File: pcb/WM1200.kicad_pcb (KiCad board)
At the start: 4 copper layers, 159 x 104 mm, 143 parts, among them Q1 BC817, Q2 BC817, Q3 BC817, Q4 BC817, Q5 BC817, Q6 BC817, U1 74LVCH162245A, U2 74LVCH162245A, U3 74LVCH162245A, U4 74LVCH162245A, U5 74LVCH162245A, U6 ADP2108AUJ-3.3, U7 TPD12S016PWR, X1 audio_expansion, X2 A1200_trapdoor_connector, X3 AC7020, X4 Conn_02x05_Odd_Even, X5 HDMI_A

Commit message: time to stop for today
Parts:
- moved C31 10.6 mm to (230.1, 111.3)
- moved R21 10.6 mm to (218.8, 113.2)
- moved R23 10.6 mm to (222.3, 122.7)
- moved C29 10.6 mm to (230.8, 120.5)
- moved C30 10.6 mm to (219.5, 119.5)
- moved C32 10.6 mm to (240.0, 108.3)
- moved R22 10.6 mm to (216.8, 116.9)
- moved R24 10.6 mm to (240.0, 106.8)
- moved R25 10.6 mm to (219.7, 116.9)
- moved U7 10.6 mm to (225.2, 116.6)
- moved X5 10.6 mm to (226.5, 113.1)
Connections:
- X3 pad J11_10: _FPGA_IPL0 -> Net-(X3-PadJ11_10)
- X3 pad J11_11: FPGA_FC1 -> Net-(X3-PadJ11_11)
- X3 pad J11_12: _FPGA_IPL1 -> Net-(X3-PadJ11_12)
- X3 pad J11_13: FPGA_FC2 -> Net-(X3-PadJ11_13)
- X3 pad J11_14: _FPGA_IPL2 -> Net-(X3-PadJ11_14)
- X3 pad J11_15: FPGA_R_W -> Net-(X3-PadJ11_15)
- X3 pad J11_16: _FPGA_RST -> Net-(X3-PadJ11_16)
- X3 pad J11_17: FPGA_SIZE0 -> Net-(X3-PadJ11_17)
- X3 pad J11_18: FPGA_CPUCLK_A -> Net-(X3-PadJ11_18)
- X3 pad J11_19: FPGA_SIZE1 -> FPGA_HDMI_D2+
- X3 pad J11_20: FPGA_OC_HLT -> Net-(X3-PadJ11_20)
- X3 pad J11_21: FPGA_HDMI_CLK- -> FPGA_HDMI_D1+
- X3 pad J11_22: FPGA_OC_INT2 -> FPGA_HDMI_D2-
- X3 pad J11_23: FPGA_HDMI_CLK+ -> FPGA_HDMI_D0+
- X3 pad J11_24: FPGA_OC_INT6 -> FPGA_HDMI_D1-
- X3 pad J11_25: FPGA_HDMI_D0- -> FPGA_HDMI_CLK+
- X3 pad J11_26: FPGA_OC_BOSS -> FPGA_HDMI_D0-
- X3 pad J11_27: FPGA_HDMI_D0+ -> Net-(X3-PadJ11_27)
- X3 pad J11_28: FPGA_OC_OVR -> FPGA_HDMI_CLK-
- X3 pad J11_29: FPGA_HDMI_D1- -> Net-(X3-PadJ11_29)
- X3 pad J11_3: FPGA_AUD_SD -> Net-(X3-PadJ11_3)
- X3 pad J11_30: FPGA_OC_RST -> Net-(X3-PadJ11_30)
- X3 pad J11_31: FPGA_HDMI_D1+ -> Net-(X3-PadJ11_31)
- X3 pad J11_32: _FPGA_DS -> Net-(X3-PadJ11_32)
- X3 pad J11_33: FPGA_HDMI_D2- -> Net-(X3-PadJ11_33)
- X3 pad J11_34: _FPGA_BERR -> Net-(X3-PadJ11_34)
- X3 pad J11_35: FPGA_HDMI_D2+ -> Net-(X3-PadJ11_35)
- X3 pad J11_36: _FPGA_AS -> Net-(X3-PadJ11_36)
- X3 pad J11_4: _FPGA_DSACK0 -> Net-(X3-PadJ11_4)
- X3 pad J11_5: FPGA_AUD_PWM_R -> Net-(X3-PadJ11_5)
- X3 pad J11_6: _FPGA_DSACK1 -> Net-(X3-PadJ11_6)
- X3 pad J11_7: FPGA_AUD_PWM_L -> Net-(X3-PadJ11_7)
- X3 pad J11_8: _FPGA_HLT -> Net-(X3-PadJ11_8)
- X3 pad J11_9: FPGA_FC0 -> Net-(X3-PadJ11_9)
- X3 pad J12_10: FPGA_D14 -> FPGA_AUD_PWM_L
- X3 pad J12_11: FPGA_D17 -> FPGA_FC2
- X3 pad J12_12: FPGA_D16 -> FPGA_AUD_SD
- X3 pad J12_13: FPGA_D19 -> FPGA_R_W
- X3 pad J12_14: FPGA_D18 -> _FPGA_DS
- X3 pad J12_15: FPGA_D21 -> FPGA_SIZE1
- X3 pad J12_16: FPGA_D20 -> _FPGA_AS
- X3 pad J12_17: FPGA_D23 -> FPGA_CPUCLK_A
- X3 pad J12_18: FPGA_D22 -> FPGA_SIZE0
- X3 pad J12_19: FPGA_D25 -> _FPGA_HLT
- X3 pad J12_20: FPGA_D24 -> _FPGA_BERR
- X3 pad J12_21: FPGA_D27 -> _FPGA_IPL0
- X3 pad J12_22: FPGA_D26 -> _FPGA_RST
- X3 pad J12_23: FPGA_D29 -> _FPGA_IPL1
- X3 pad J12_24: FPGA_D28 -> _FPGA_IPL2
- X3 pad J12_25: FPGA_D31 -> _FPGA_DSACK1
- X3 pad J12_26: FPGA_D30 -> _FPGA_DSACK0
- X3 pad J12_27: _FPGA_D_BUFF_OE -> Net-(X3-PadJ12_27)
- X3 pad J12_28: FPGA_D_BUFF_DIR -> Net-(X3-PadJ12_28)
- X3 pad J12_29: FPGA_D1 -> Net-(X3-PadJ12_29)
- X3 pad J12_3: FPGA_D9 -> FPGA_OC_BOSS
- X3 pad J12_30: FPGA_D0 -> Net-(X3-PadJ12_30)
- X3 pad J12_31: FPGA_D3 -> Net-(X3-PadJ12_31)
- X3 pad J12_32: FPGA_D2 -> Net-(X3-PadJ12_32)
- X3 pad J12_33: FPGA_D5 -> Net-(X3-PadJ12_33)
- X3 pad J12_34: FPGA_D4 -> Net-(X3-PadJ12_34)
- X3 pad J12_35: FPGA_D7 -> Net-(X3-PadJ12_35)
- X3 pad J12_36: FPGA_D6 -> Net-(X3-PadJ12_36)
- X3 pad J12_4: FPGA_D8 -> FPGA_OC_OVR
- X3 pad J12_5: FPGA_D11 -> FPGA_OC_INT6
- X3 pad J12_6: FPGA_D10 -> FPGA_OC_INT2
- X3 pad J12_7: FPGA_D13 -> FPGA_FC0
- X3 pad J12_8: FPGA_D12 -> FPGA_AUD_PWM_R
- X3 pad J12_9: FPGA_D15 -> FPGA_FC1
- XT49 pad 1: Net-(XT49-Pad1) -> FPGA_OC_HLT
- XT51 pad 1: Net-(XT51-Pad1) -> FPGA_OC_BOSS
- XT53 pad 1: Net-(XT53-Pad1) -> FPGA_OC_INT6
- XT55 pad 1: Net-(XT55-Pad1) -> FPGA_OC_RST
- XT57 pad 1: Net-(XT57-Pad1) -> FPGA_OC_INT2
- XT59 pad 1: Net-(XT59-Pad1) -> FPGA_OC_OVR
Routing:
- net FPGA_D_BUFF_DIR: track 113.8 -> 33.6 mm, vias 3 -> 2
- net _FPGA_D_BUFF_OE: track 112.0 -> 33.1 mm, vias 3 -> 2
- net FPGA_D6: track 78.7 -> 0.00 mm
- net FPGA_D7: track 77.4 -> 0.00 mm
- net FPGA_D4: track 76.0 -> 0.00 mm
- net FPGA_D30: track 75.7 -> 0.00 mm
- net FPGA_D5: track 74.7 -> 0.00 mm
- net FPGA_D31: track 73.9 -> 0.00 mm
- net FPGA_D2: track 73.3 -> 0.00 mm
- net FPGA_D28: track 72.7 -> 0.00 mm
- net FPGA_D3: track 71.4 -> 0.00 mm
- net FPGA_D29: track 70.8 -> 0.00 mm
- net FPGA_D0: track 70.7 -> 0.00 mm
- net FPGA_D1: track 69.4 -> 0.00 mm
- net FPGA_D26: track 69.4 -> 0.00 mm
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
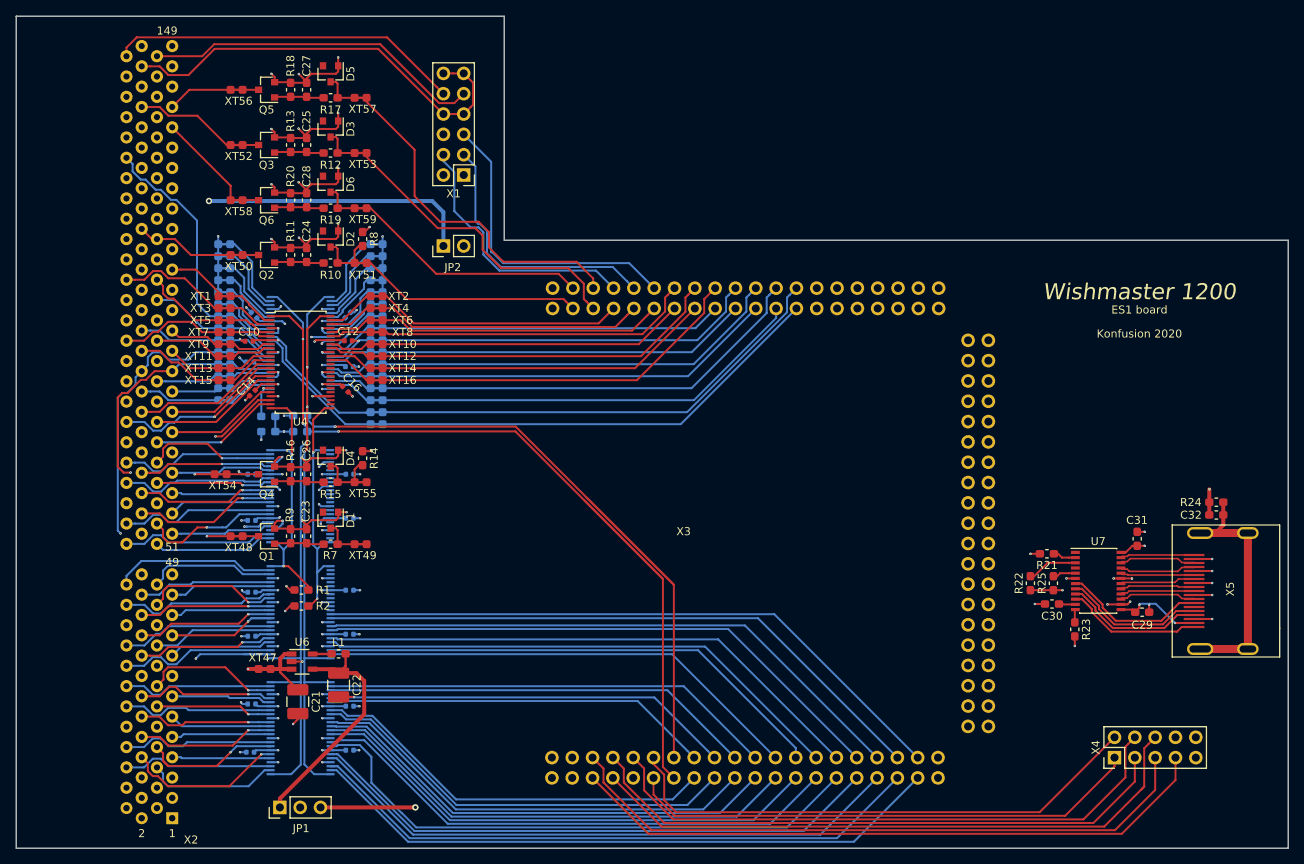
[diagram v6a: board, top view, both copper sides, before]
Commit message: wire length aligns
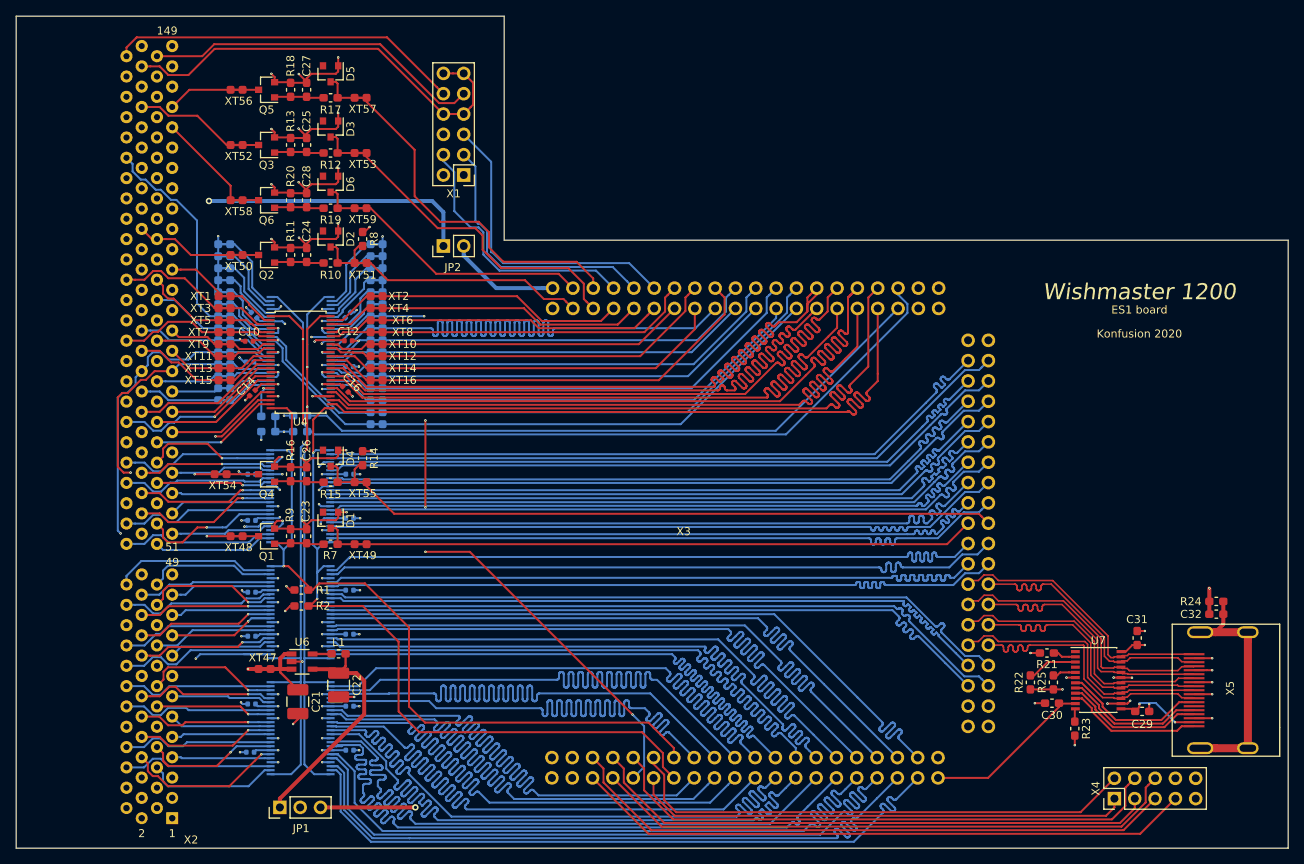
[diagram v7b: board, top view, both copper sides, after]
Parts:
- moved C29 12.4 mm to (230.8, 132.9)
- moved C30 12.4 mm to (219.5, 131.9)
- moved C32 12.4 mm to (240.0, 120.7)
- moved R22 12.4 mm to (216.8, 129.3)
- moved R23 12.4 mm to (222.3, 135.1)
- moved R24 12.4 mm to (240.0, 119.2)
- moved R25 12.4 mm to (219.7, 129.3)
- moved U7 12.4 mm to (225.2, 129.0)
- moved X5 12.4 mm to (226.5, 125.5)
- moved C31 12.4 mm to (230.1, 123.7)
- moved R21 12.4 mm to (218.8, 125.6)
- moved X4 5.12 mm to (227.3, 143.8)
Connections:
- X3 pad J10_27: _FPGA_A_BUFF_OE -> FPGA_D_BUFF_DIR
- X3 pad J10_28: FPGA_A_BUFF_DIR -> _FPGA_D_BUFF_OE
- X3 pad J11_10: Net-(X3-PadJ11_10) -> FPGA_D15
- X3 pad J11_11: Net-(X3-PadJ11_11) -> FPGA_D16
- X3 pad J11_12: Net-(X3-PadJ11_12) -> FPGA_D17
- X3 pad J11_13: Net-(X3-PadJ11_13) -> FPGA_D18
- X3 pad J11_14: Net-(X3-PadJ11_14) -> FPGA_D19
- X3 pad J11_15: Net-(X3-PadJ11_15) -> FPGA_D20
- X3 pad J11_16: Net-(X3-PadJ11_16) -> FPGA_D21
- X3 pad J11_17: Net-(X3-PadJ11_17) -> FPGA_D22
- X3 pad J11_18: Net-(X3-PadJ11_18) -> FPGA_D23
- X3 pad J11_19: FPGA_HDMI_D2+ -> FPGA_OC_HLT
- X3 pad J11_2: FPGA_VCC5V -> Net-(X3-PadJ11_2)
- X3 pad J11_20: Net-(X3-PadJ11_20) -> FPGA_OC_RST
- X3 pad J11_21: FPGA_HDMI_D1+ -> FPGA_D24
- X3 pad J11_22: FPGA_HDMI_D2- -> FPGA_D25
- X3 pad J11_23: FPGA_HDMI_D0+ -> FPGA_D26
- X3 pad J11_24: FPGA_HDMI_D1- -> FPGA_D27
- X3 pad J11_25: FPGA_HDMI_CLK+ -> FPGA_HDMI_D2+
- X3 pad J11_26: FPGA_HDMI_D0- -> FPGA_HDMI_D2-
- X3 pad J11_27: Net-(X3-PadJ11_27) -> FPGA_HDMI_D1+
- X3 pad J11_28: FPGA_HDMI_CLK- -> FPGA_HDMI_D1-
- X3 pad J11_29: Net-(X3-PadJ11_29) -> FPGA_HDMI_D0+
- X3 pad J11_3: Net-(X3-PadJ11_3) -> FPGA_D8
- X3 pad J11_30: Net-(X3-PadJ11_30) -> FPGA_HDMI_D0-
- X3 pad J11_31: Net-(X3-PadJ11_31) -> FPGA_HDMI_CLK+
- X3 pad J11_32: Net-(X3-PadJ11_32) -> FPGA_HDMI_CLK-
- X3 pad J11_33: Net-(X3-PadJ11_33) -> FPGA_D29
- X3 pad J11_34: Net-(X3-PadJ11_34) -> FPGA_D28
- X3 pad J11_35: Net-(X3-PadJ11_35) -> FPGA_D31
- X3 pad J11_36: Net-(X3-PadJ11_36) -> FPGA_D30
- X3 pad J11_4: Net-(X3-PadJ11_4) -> FPGA_D9
- X3 pad J11_5: Net-(X3-PadJ11_5) -> FPGA_D10
- X3 pad J11_6: Net-(X3-PadJ11_6) -> FPGA_D11
- X3 pad J11_7: Net-(X3-PadJ11_7) -> FPGA_D12
- X3 pad J11_8: Net-(X3-PadJ11_8) -> FPGA_D13
- X3 pad J11_9: Net-(X3-PadJ11_9) -> FPGA_D14
- X3 pad J12_27: Net-(X3-PadJ12_27) -> FPGA_D1
- X3 pad J12_28: Net-(X3-PadJ12_28) -> FPGA_D0
- X3 pad J12_29: Net-(X3-PadJ12_29) -> FPGA_D3
- X3 pad J12_30: Net-(X3-PadJ12_30) -> FPGA_D2
- X3 pad J12_31: Net-(X3-PadJ12_31) -> FPGA_D5
- X3 pad J12_32: Net-(X3-PadJ12_32) -> FPGA_D4
- X3 pad J12_33: Net-(X3-PadJ12_33) -> FPGA_D7
- X3 pad J12_34: Net-(X3-PadJ12_34) -> FPGA_D6
- X3 pad J12_35: Net-(X3-PadJ12_35) -> _FPGA_A_BUFF_OE
- X3 pad J12_36: Net-(X3-PadJ12_36) -> FPGA_A_BUFF_DIR
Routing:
- net FPGA_D0: track 0.00 -> 94.2 mm
- net FPGA_D4: track 0.00 -> 90.6 mm
- net FPGA_D8: track 0.00 -> 87.5 mm
- net FPGA_D5: track 0.00 -> 87.4 mm
- net FPGA_D11: track 0.00 -> 87.4 mm
- net FPGA_D14: track 0.00 -> 87.4 mm
- net FPGA_D27: track 0.00 -> 87.4 mm
- net FPGA_D20: track 0.00 -> 87.4 mm
- net FPGA_D30: track 0.00 -> 87.4 mm
- net FPGA_D26: track 0.00 -> 87.3 mm
- net FPGA_D15: track 0.00 -> 87.3 mm
- net FPGA_D16: track 0.00 -> 87.3 mm
- net FPGA_D9: track 0.00 -> 87.3 mm
- net FPGA_D25: track 0.00 -> 87.3 mm
- net FPGA_D29: track 0.00 -> 87.3 mm
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
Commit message: Some more work done
I'm too lazy to think about commit messages in my pet project, really
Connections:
- C30 pad 1: FPGA_VCC5V -> FPGA_VCC5V_1
- JP2 pad 2: FPGA_VCC5V -> FPGA_VCC5V_2
- U7 pad 11: FPGA_VCC5V -> FPGA_VCC5V_1
- X3 pad J10_2: FPGA_VCC5V -> FPGA_VCC5V_1
- X3 pad J12_2: FPGA_VCC5V -> FPGA_VCC5V_2
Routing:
- net FPGA_CPUCLK_A: track 85.0 -> 42.6 mm
- net FPGA_VCC5V: track 35.3 -> 0.00 mm
- net FPGA_VCC5V_1: track 0.00 -> 21.3 mm
- net FPGA_VCC5V_2: track 0.00 -> 14.0 mm
- net FPGA_A16: track 87.3 -> 76.1 mm
- net FPGA_A6: track 87.4 -> 83.1 mm
- net FPGA_A1: track 87.3 -> 83.0 mm
- net FPGA_A17: track 87.3 -> 83.1 mm
- net FPGA_A4: track 87.3 -> 83.1 mm
- net FPGA_A22: track 88.2 -> 84.0 mm
- net FPGA_A18: track 87.3 -> 83.1 mm
- net FPGA_A21: track 88.1 -> 83.8 mm
- net FPGA_A7: track 87.3 -> 83.1 mm
- net FPGA_A9: track 87.3 -> 83.1 mm
- net FPGA_A2: track 87.3 -> 83.1 mm
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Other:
- board text added: "In me the Wishmaster"
- board text added: "TODO: replace all microvias with ordinary (yet small) vias"
